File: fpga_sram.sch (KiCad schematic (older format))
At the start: 1 part

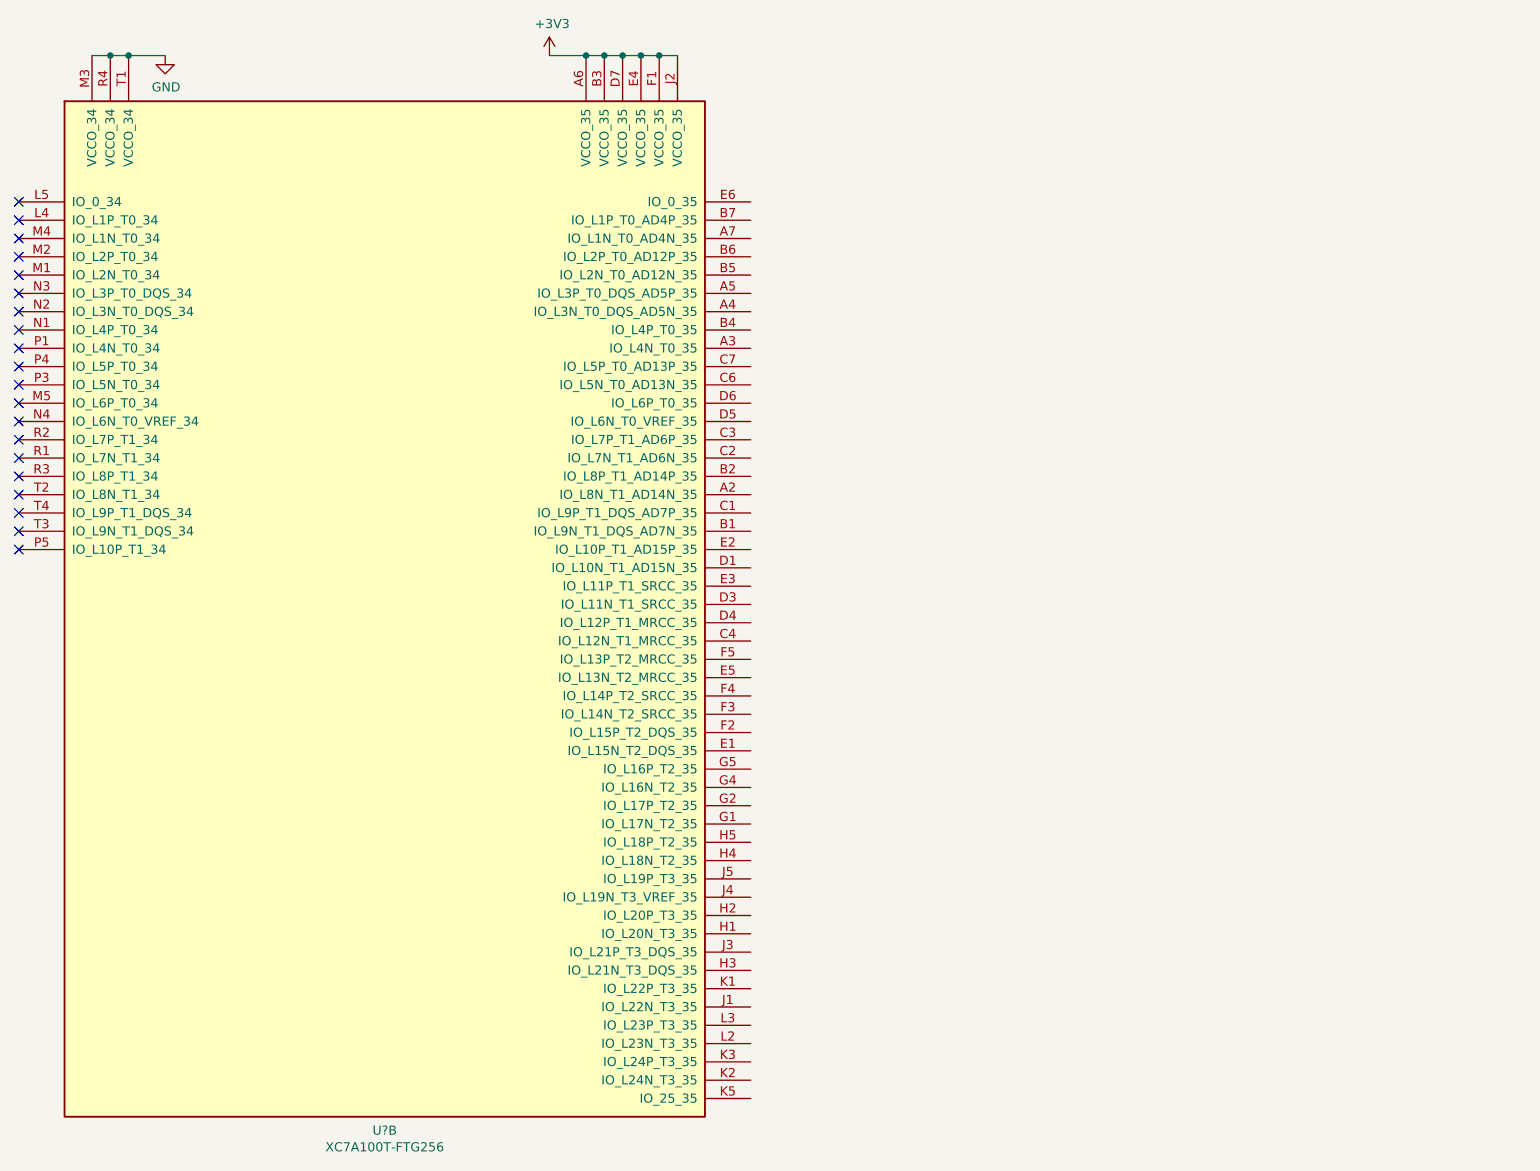
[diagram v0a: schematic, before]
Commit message: Connect SRAM and FPGA
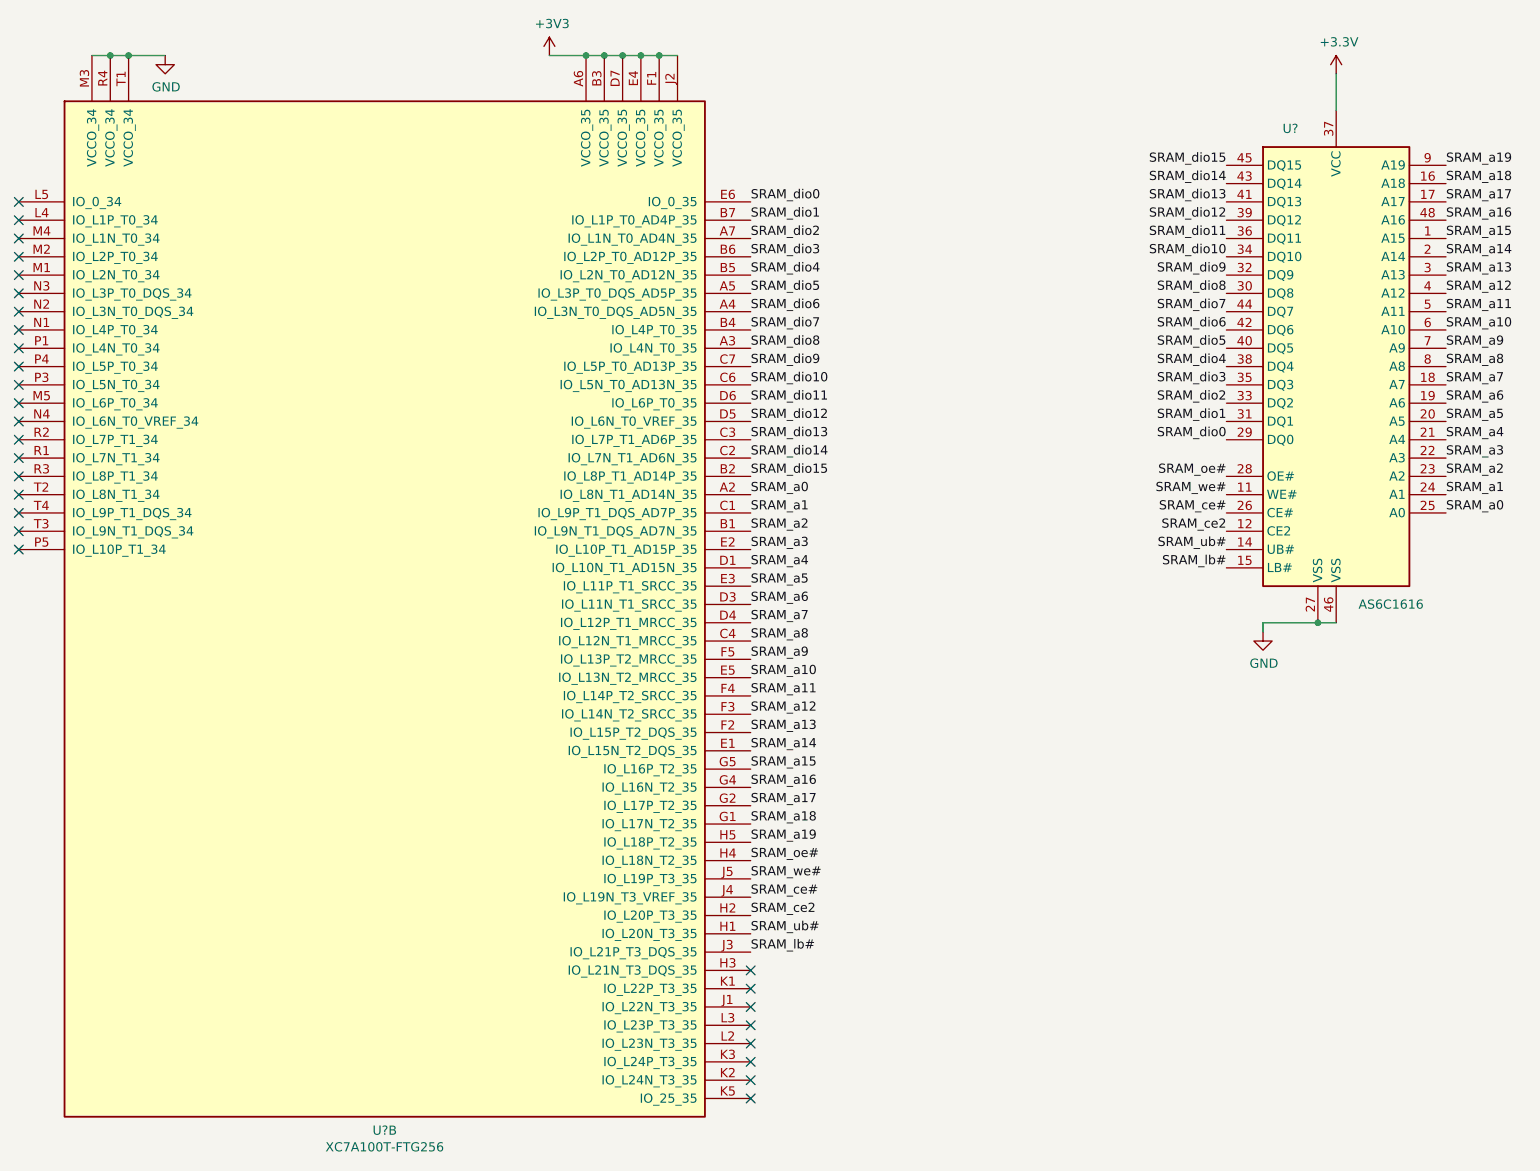
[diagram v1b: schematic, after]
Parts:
- added U?: AS6C1616, Package_SO:TSOP-I-48_18.4x12mm_P0.5mm, symbol Memory_RAM:AS6C1616
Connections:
- net +3V3: now also U?.37 (VCC)
- net GND: now also U?.27 (VSS), U?.46 (VSS)
- net SRAM_a0: now reaches U?.A2 (IO_L8N_T1_AD14N_35)
- net SRAM_a0: now also U?.25 (A0)
- net SRAM_dio8: now reaches U?.A3 (IO_L4N_T0_35)
- net SRAM_dio8: now also U?.30 (DQ8)
- net SRAM_dio6: now reaches U?.A4 (IO_L3N_T0_DQS_AD5N_35)
- net SRAM_dio6: now also U?.42 (DQ6)
- net SRAM_dio5: now reaches U?.A5 (IO_L3P_T0_DQS_AD5P_35)
- net SRAM_dio5: now also U?.40 (DQ5)
- net SRAM_dio2: now reaches U?.A7 (IO_L1N_T0_AD4N_35)
- net SRAM_dio2: now also U?.33 (DQ2)
- net SRAM_a2: now reaches U?.B1 (IO_L9N_T1_DQS_AD7N_35)
- net SRAM_a2: now also U?.23 (A2)
- net SRAM_dio15: now reaches U?.B2 (IO_L8P_T1_AD14P_35)
- net SRAM_dio15: now also U?.45 (DQ15)
- net SRAM_dio7: now reaches U?.B4 (IO_L4P_T0_35)
- net SRAM_dio7: now also U?.44 (DQ7)
- net SRAM_dio4: now reaches U?.B5 (IO_L2N_T0_AD12N_35)
- net SRAM_dio4: now also U?.38 (DQ4)
- net SRAM_dio3: now reaches U?.B6 (IO_L2P_T0_AD12P_35)
- net SRAM_dio3: now also U?.35 (DQ3)
- net SRAM_dio1: now reaches U?.B7 (IO_L1P_T0_AD4P_35)
- net SRAM_dio1: now also U?.31 (DQ1)
- net SRAM_a1: now reaches U?.C1 (IO_L9P_T1_DQS_AD7P_35)
- net SRAM_a1: now also U?.24 (A1)
- net SRAM_dio14: now reaches U?.C2 (IO_L7N_T1_AD6N_35)
- net SRAM_dio14: now also U?.43 (DQ14)
- net SRAM_dio13: now reaches U?.C3 (IO_L7P_T1_AD6P_35)
- net SRAM_dio13: now also U?.41 (DQ13)
- net SRAM_a8: now reaches U?.C4 (IO_L12N_T1_MRCC_35)
- net SRAM_a8: now also U?.8 (A8)
- net SRAM_dio10: now reaches U?.C6 (IO_L5N_T0_AD13N_35)
- net SRAM_dio10: now also U?.34 (DQ10)
- net SRAM_dio9: now reaches U?.C7 (IO_L5P_T0_AD13P_35)
- net SRAM_dio9: now also U?.32 (DQ9)
- net SRAM_a4: now reaches U?.D1 (IO_L10N_T1_AD15N_35)
- net SRAM_a4: now also U?.21 (A4)
- net SRAM_a6: now reaches U?.D3 (IO_L11N_T1_SRCC_35)
- net SRAM_a6: now also U?.19 (A6)
- net SRAM_a7: now reaches U?.D4 (IO_L12P_T1_MRCC_35)
- net SRAM_a7: now also U?.18 (A7)
- net SRAM_dio12: now reaches U?.D5 (IO_L6N_T0_VREF_35)
- net SRAM_dio12: now also U?.39 (DQ12)
- net SRAM_dio11: now reaches U?.D6 (IO_L6P_T0_35)
- net SRAM_dio11: now also U?.36 (DQ11)
- net SRAM_a14: now reaches U?.E1 (IO_L15N_T2_DQS_35)
- net SRAM_a14: now also U?.2 (A14)
- net SRAM_a3: now reaches U?.E2 (IO_L10P_T1_AD15P_35)
- net SRAM_a3: now also U?.22 (A3)
- net SRAM_a5: now reaches U?.E3 (IO_L11P_T1_SRCC_35)
- net SRAM_a5: now also U?.20 (A5)
- net SRAM_a10: now reaches U?.E5 (IO_L13N_T2_MRCC_35)
- net SRAM_a10: now also U?.6 (A10)
- net SRAM_dio0: now reaches U?.E6 (IO_0_35)
- net SRAM_dio0: now also U?.29 (DQ0)
- net SRAM_a13: now reaches U?.F2 (IO_L15P_T2_DQS_35)
- net SRAM_a13: now also U?.3 (A13)
- net SRAM_a12: now reaches U?.F3 (IO_L14N_T2_SRCC_35)
- net SRAM_a12: now also U?.4 (A12)
- net SRAM_a11: now reaches U?.F4 (IO_L14P_T2_SRCC_35)
- net SRAM_a11: now also U?.5 (A11)
- net SRAM_a9: now reaches U?.F5 (IO_L13P_T2_MRCC_35)
- net SRAM_a9: now also U?.7 (A9)
- net SRAM_a18: now reaches U?.G1 (IO_L17N_T2_35)
- net SRAM_a18: now also U?.16 (A18)
- net SRAM_a17: now reaches U?.G2 (IO_L17P_T2_35)
- net SRAM_a17: now also U?.17 (A17)
- net SRAM_a16: now reaches U?.G4 (IO_L16N_T2_35)
- net SRAM_a16: now also U?.48 (A16)
- net SRAM_a15: now reaches U?.G5 (IO_L16P_T2_35)
- net SRAM_a15: now also U?.1 (A15)
- net SRAM_ub#: now reaches U?.H1 (IO_L20N_T3_35)
- net SRAM_ub#: now also U?.14 (UB#)
- net SRAM_ce2: now reaches U?.H2 (IO_L20P_T3_35)
- net SRAM_ce2: now also U?.12 (CE2)
- net SRAM_oe#: now reaches U?.H4 (IO_L18N_T2_35)
- net SRAM_oe#: now also U?.28 (OE#)
- net SRAM_a19: now reaches U?.H5 (IO_L18P_T2_35)
- net SRAM_a19: now also U?.9 (A19)
- net SRAM_lb#: now reaches U?.J3 (IO_L21P_T3_DQS_35)
- net SRAM_lb#: now also U?.15 (LB#)
- net SRAM_ce#: now reaches U?.J4 (IO_L19N_T3_VREF_35)
- net SRAM_ce#: now also U?.26 (CE#)
- net SRAM_we#: now reaches U?.J5 (IO_L19P_T3_35)
- net SRAM_we#: now also U?.11 (WE#)
- no-connect marks 20 -> 28
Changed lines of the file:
@@
 AR Path="/5D7D43D9/5E114C44" Ref="#PWR?"  Part="1"
 AR Path="/5D7D43D9/5DD5155F/5E114C44" Ref="#PWR?"  Part="1"
+AR Path="/5D7D43D9/5E0EF1ED/5E114C44" Ref="#PWR?"  Part="1"
 F 0 "#PWR?" H 2700 550 50  0001 C CNN
 F 1 "GND" H 2705 627 50  0000 C CNN
@@
 	1    0    0    -1
 $EndComp
+Connection ~ 2400 800
+Wire Wire Line
+	2300 800  2400 800
+Connection ~ 2500 800
+Wire Wire Line
+	2400 800  2500 800
+Wire Wire Line
+	2500 800  2700 800
+Connection ~ 5000 800
+Wire Wire Line
+	5000 800  5100 800
+Wire Wire Line
+	4800 800  5000 800
+Connection ~ 5100 800
+Connection ~ 5200 800
+Wire Wire Line
+	5100 800  5200 800
+Wire Wire Line
+	5200 800  5300 800
+Connection ~ 5300 800
+Connection ~ 5400 800
+Wire Wire Line
+	5300 800  5400 800
 Wire Wire Line
 	5400 800  5500 800
-Connection ~ 5400 800
-Wire Wire Line
-	5300 800  5400 800
-Connection ~ 5300 800
-Wire Wire Line
-	5200 800  5300 800
-Connection ~ 5200 800
-Wire Wire Line
-	5100 800  5200 800
-Connection ~ 5100 800
-Wire Wire Line
-	4800 800  5000 800
-Wire Wire Line
-	5000 800  5100 800
-Connection ~ 5000 800
-Wire Wire Line
-	2500 800  2700 800
-Connection ~ 2500 800
-Wire Wire Line
-	2300 800  2400 800
-Wire Wire Line
-	2400 800  2500 800
-Connection ~ 2400 800
 $Comp
 L FPGA_Xilinx_Artix7:XC7A100T-FTG256 U?
@@
 	1    0    0    -1
 $EndComp
+Text Label 8500 2900 2    50   ~ 0
+SRAM_dio0
+Text Label 8500 2800 2    50   ~ 0
+SRAM_dio1
+Text Label 8500 2700 2    50   ~ 0
+SRAM_dio2
+Text Label 8500 2600 2    50   ~ 0
+SRAM_dio3
+Text Label 8500 2500 2    50   ~ 0
+SRAM_dio4
+Text Label 8500 2400 2    50   ~ 0
+SRAM_dio5
+Text Label 8500 2300 2    50   ~ 0
+SRAM_dio6
+Text Label 8500 2200 2    50   ~ 0
+SRAM_dio7
+Text Label 8500 2100 2    50   ~ 0
+SRAM_dio8
+Text Label 8500 2000 2    50   ~ 0
+SRAM_dio9
+Text Label 8500 1900 2    50   ~ 0
+SRAM_dio10
+Text Label 8500 1800 2    50   ~ 0
+SRAM_dio11
+Text Label 8500 1700 2    50   ~ 0
+SRAM_dio12
+Text Label 8500 1600 2    50   ~ 0
+SRAM_dio13
+Text Label 8500 1500 2    50   ~ 0
+SRAM_dio14
+Text Label 8500 1400 2    50   ~ 0
+SRAM_dio15
+Text Label 5900 1600 0    50   ~ 0
+SRAM_dio0
+Text Label 5900 1700 0    50   ~ 0
+SRAM_dio1
+Text Label 5900 1800 0    50   ~ 0
+SRAM_dio2
+Text Label 5900 1900 0    50   ~ 0
+SRAM_dio3
+Text Label 5900 2000 0    50   ~ 0
+SRAM_dio4
+Text Label 5900 2100 0    50   ~ 0
+SRAM_dio5
+Text Label 5900 2200 0    50   ~ 0
+SRAM_dio6
+Text Label 5900 2300 0    50   ~ 0
+SRAM_dio7
+Text Label 5900 2400 0    50   ~ 0
+SRAM_dio8
+Text Label 5900 2500 0    50   ~ 0
+SRAM_dio9
+Text Label 5900 2600 0    50   ~ 0
+SRAM_dio10
+Text Label 5900 2700 0    50   ~ 0
+SRAM_dio11
+Text Label 5900 2800 0    50   ~ 0
+SRAM_dio12
+Text Label 5900 2900 0    50   ~ 0
+SRAM_dio13
+Text Label 5900 3000 0    50   ~ 0
+SRAM_dio14
+Text Label 5900 3100 0    50   ~ 0
+SRAM_dio15
+Text Label 9700 3300 0    50   ~ 0
+SRAM_a0
+Text Label 9700 3200 0    50   ~ 0
+SRAM_a1
+Text Label 9700 3100 0    50   ~ 0
+SRAM_a2
+Text Label 9700 3000 0    50   ~ 0
+SRAM_a3
+Text Label 9700 2900 0    50   ~ 0
+SRAM_a4
+Text Label 9700 2800 0    50   ~ 0
+SRAM_a5
+Text Label 9700 2700 0    50   ~ 0
+SRAM_a6
+Text Label 9700 2600 0    50   ~ 0
+SRAM_a7
+Text Label 9700 2500 0    50   ~ 0
+SRAM_a8
+Text Label 9700 2400 0    50   ~ 0
+SRAM_a9
+Text Label 9700 2300 0    50   ~ 0
+SRAM_a10
+Text Label 9700 2200 0    50   ~ 0
+SRAM_a11
+Text Label 9700 2100 0    50   ~ 0
+SRAM_a12
+Text Label 9700 2000 0    50   ~ 0
+SRAM_a13
+Text Label 9700 1900 0    50   ~ 0
+SRAM_a14
+Text Label 9700 1800 0    50   ~ 0
+SRAM_a15
+Text Label 9700 1700 0    50   ~ 0
+SRAM_a16
+Text Label 9700 1600 0    50   ~ 0
+SRAM_a17
+Text Label 9700 1500 0    50   ~ 0
+SRAM_a18
+Text Label 9700 1400 0    50   ~ 0
+SRAM_a19
+Text Label 5900 3200 0    50   ~ 0
+SRAM_a0
+Text Label 5900 3300 0    50   ~ 0
+SRAM_a1
+Text Label 5900 3400 0    50   ~ 0
+SRAM_a2
+Text Label 5900 3500 0    50   ~ 0
+SRAM_a3
+Text Label 5900 3600 0    50   ~ 0
+SRAM_a4
+Text Label 5900 3700 0    50   ~ 0
+SRAM_a5
+Text Label 5900 3800 0    50   ~ 0
+SRAM_a6
+Text Label 5900 3900 0    50   ~ 0
+SRAM_a7
+Text Label 5900 4000 0    50   ~ 0
+SRAM_a8
+Text Label 5900 4100 0    50   ~ 0
+SRAM_a9
+Text Label 5900 4200 0    50   ~ 0
+SRAM_a10
+Text Label 5900 4300 0    50   ~ 0
+SRAM_a11
+Text Label 5900 4400 0    50   ~ 0
+SRAM_a12
+Text Label 5900 4500 0    50   ~ 0
+SRAM_a13
+Text Label 5900 4600 0    50   ~ 0
+SRAM_a14
+Text Label 5900 4700 0    50   ~ 0
+SRAM_a15
+Text Label 5900 4800 0    50   ~ 0
+SRAM_a16
+Text Label 5900 4900 0    50   ~ 0
+SRAM_a17
+Text Label 5900 5000 0    50   ~ 0
+SRAM_a18
+Text Label 5900 5100 0    50   ~ 0
+SRAM_a19
+$Comp
+L Memory_RAM:AS6C1616 U?
+U 1 1 5D9286C8
+P 9100 2500
+F 0 "U?" H 8850 3800 50  0000 C CNN
+F 1 "AS6C1616" H 9400 1200 50  0000 C CNN
+F 2 "Package_SO:TSOP-I-48_18.4x12mm_P0.5mm" H 10150 1150 50  0001 C CNN
+F 3 "https://www.alliancememory.com/wp-content/uploads/pdf/AS6C1616-TSOPI.pdf" H 8800 2950 50  0001 C CNN
+	1    9100 2500
+	1    0    0    -1
+$EndComp
+Text Label 8500 3100 2    50   ~ 0
+SRAM_oe#
+Text Label 8500 3200 2    50   ~ 0
+SRAM_we#
+Text Label 8500 3300 2    50   ~ 0
+SRAM_ce#
+Text Label 8500 3400 2    50   ~ 0
+SRAM_ce2
+Text Label 8500 3500 2    50   ~ 0
+SRAM_ub#
+Text Label 8500 3600 2    50   ~ 0
+SRAM_lb#
+Text Label 5900 5200 0    50   ~ 0
+SRAM_oe#
+Text Label 5900 5300 0    50   ~ 0
+SRAM_we#
+Text Label 5900 5400 0    50   ~ 0
+SRAM_ce#
+Text Label 5900 5500 0    50   ~ 0
+SRAM_ce2
+Text Label 5900 5600 0    50   ~ 0
+SRAM_ub#
+Text Label 5900 5700 0    50   ~ 0
+SRAM_lb#
+$Comp
+L power:+3.3V #PWR?
+U 1 1 5DA6CE44
+P 9100 900
+F 0 "#PWR?" H 9100 750 50  0001 C CNN
+F 1 "+3.3V" H 9115 1073 50  0000 C CNN
+F 2 "" H 9100 900 50  0001 C CNN
+F 3 "" H 9100 900 50  0001 C CNN
+	1    9100 900
+	1    0    0    -1
+$EndComp
+Wire Wire Line
+	9100 900  9100 1100
+$Comp
+L power:GND #PWR?
+U 1 1 5DA73B0A
+P 8700 3950
+F 0 "#PWR?" H 8700 3700 50  0001 C CNN
+F 1 "GND" H 8705 3777 50  0000 C CNN
+F 2 "" H 8700 3950 50  0001 C CNN
+F 3 "" H 8700 3950 50  0001 C CNN
+	1    8700 3950
+	1    0    0    -1
+$EndComp
+Wire Wire Line
+	9100 3900 9000 3900
+Wire Wire Line
+	8700 3900 8700 3950
+Connection ~ 9000 3900
+Wire Wire Line
+	9000 3900 8700 3900
+NoConn ~ 5900 5800
+NoConn ~ 5900 5900
+NoConn ~ 5900 6000
+NoConn ~ 5900 6100
+NoConn ~ 5900 6200
+NoConn ~ 5900 6300
+NoConn ~ 5900 6400
+NoConn ~ 5900 6500
 $EndSCHEMATC

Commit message: Change power symbol
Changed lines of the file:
@@
 Text Label 5900 5700 0    50   ~ 0
 SRAM_lb#
-$Comp
-L power:+3.3V #PWR?
-U 1 1 5DA6CE44
-P 9100 900
-F 0 "#PWR?" H 9100 750 50  0001 C CNN
-F 1 "+3.3V" H 9115 1073 50  0000 C CNN
-F 2 "" H 9100 900 50  0001 C CNN
-F 3 "" H 9100 900 50  0001 C CNN
-	1    9100 900
-	1    0    0    -1
-$EndComp
 Wire Wire Line
 	9100 900  9100 1100
@@
 NoConn ~ 5900 6400
 NoConn ~ 5900 6500
+$Comp
+L power:+3V3 #PWR?
+U 1 1 5DB40E20
+P 9100 900
+F 0 "#PWR?" H 9100 750 50  0001 C CNN
+F 1 "+3V3" H 9115 1073 50  0000 C CNN
+F 2 "" H 9100 900 50  0001 C CNN
+F 3 "" H 9100 900 50  0001 C CNN
+	1    9100 900
+	1    0    0    -1
+$EndComp
 $EndSCHEMATC
